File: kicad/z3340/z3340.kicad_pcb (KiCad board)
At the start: 4 copper layers, 80 x 80 mm, 152 parts, among them J1 Conn_01x01, J2 Conn_01x02, J3 Conn_02x20_Odd_Even, Q1 2N7002, Q2 2N7002, Q3 MMBT3904, U1 DG442CY+, U10 AS3364, U11 PCA9555D, U12 AD5328, U13 TL074, U14 DG406, U15 M24C02-WMN, U2 AS3340, U3 LM79L05, U4 LM311, U5 TL074, U6 LM4040AIM3-2.5, U7 LM4040B-5, U8 DG442CY+, U9 TL072

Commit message: continue file renaming
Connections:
- net /cem3340/COMP_OUT renamed /vco3340/COMP_OUT
- net /cem3340/HARD_SYNC renamed /vco3340/HARD_SYNC
- net /cem3340/HIGH_FREQ_TRACK renamed /vco3340/HIGH_FREQ_TRACK
- net /cem3340/LINEAR_FM renamed /vco3340/LINEAR_FM
- net /cem3340/PWM renamed /vco3340/PWM
- net /cem3340/SOFT_SYNC renamed /vco3340/SOFT_SYNC
- net /cem3340/SUMMING_INPUT renamed /vco3340/SUMMING_INPUT
- net /cem3340/VREF_5 renamed /vco3340/VREF_5

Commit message: z3340 v0.8 RTM
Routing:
- net GND: track 206.2 -> 203.9 mm, vias 79 -> 81
- net /VCO_PULSE: track 79.0 -> 77.7 mm
- net -12V: track 55.8 -> 55.0 mm
- net /VCO_SAW: track 74.2 -> 74.8 mm
- net +12V: track 44.4 -> 43.8 mm
- net /DAC/PWM_FROM_DAC: track 30.4 -> 30.9 mm

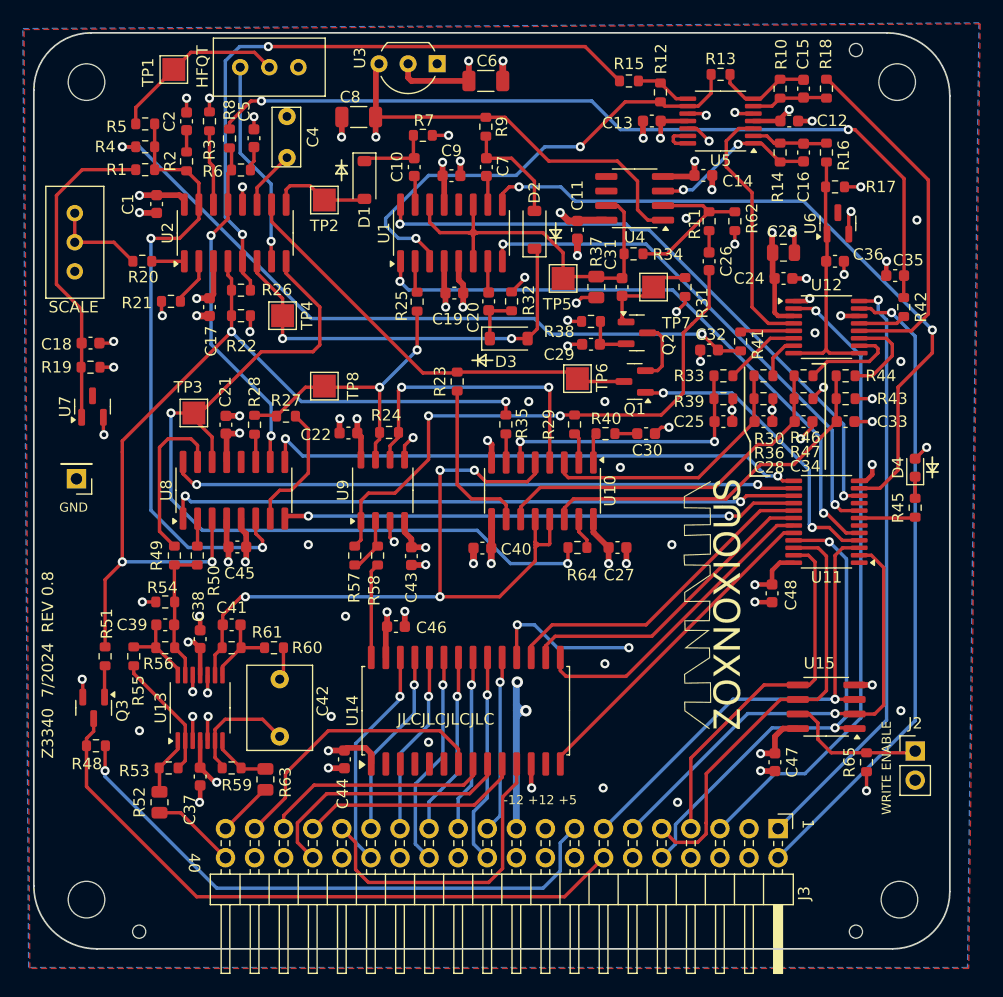
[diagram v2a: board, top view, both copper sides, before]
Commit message: checkpoint for z3340 v0.9.  Fixed lm4040 resistor, exp modulation level; removed polygons from routing
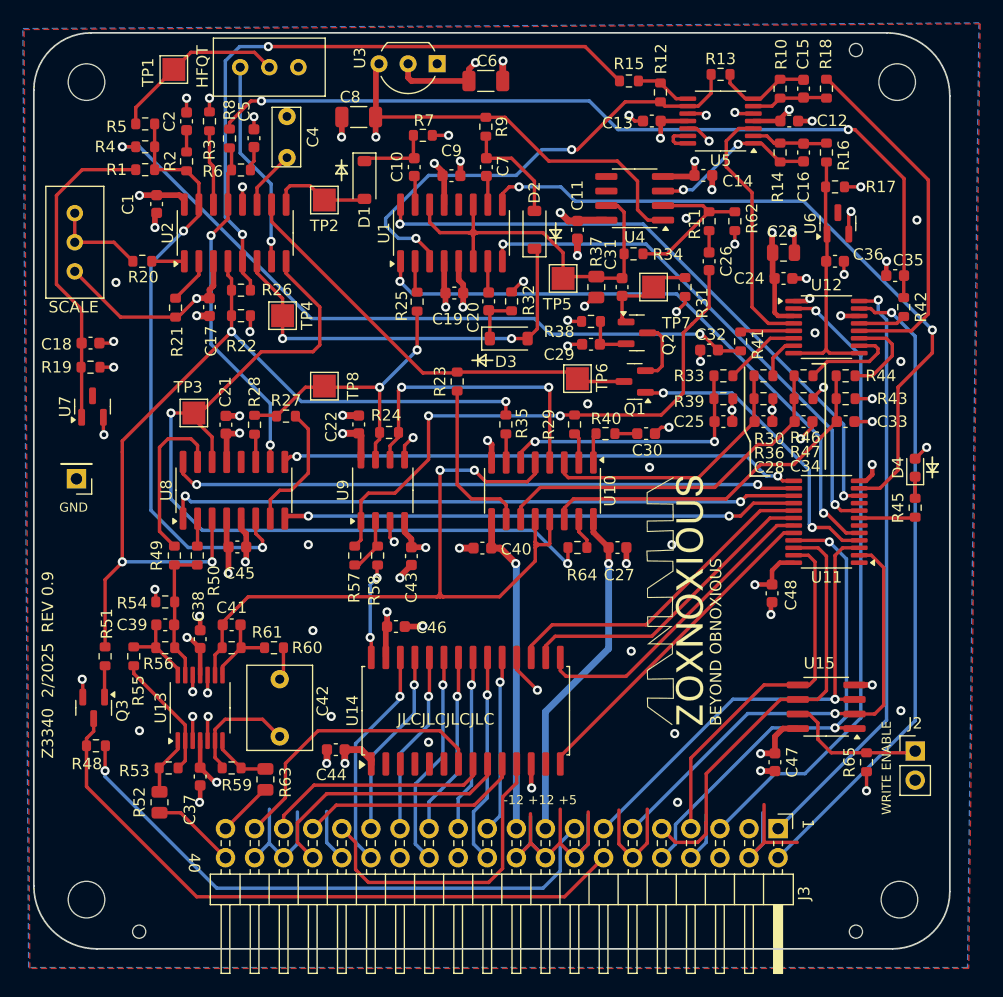
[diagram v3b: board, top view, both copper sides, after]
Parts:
- R17: value 12k -> 10k
- R27: value 200k -> 47k
- R28: value 300k -> 100k
- moved G*** 3.27 mm to (154.6, 120.0)
- moved C22 1.17 mm to (127.0, 104.6), turned to 90 degrees
- moved C44 1.13 mm to (125.0, 133.0), turned to 180 degrees
- moved R21 0.68 mm to (111.0, 94.4), turned to -90 degrees
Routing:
- net +12V: track 43.8 -> 266.8 mm
- net -12V: track 55.0 -> 171.1 mm, vias 11 -> 9
- net GND: track 203.9 -> 314.3 mm, vias 81 -> 80
- net +5V: track 88.1 -> 192.0 mm, vias 9 -> 8
- net -5V: track 42.6 -> 76.5 mm, vias 3 -> 2
- net /LINEAR_FM_EXT_CTRL: track 48.0 -> 45.6 mm
- net /vco3340/SUMMING_INPUT: track 54.0 -> 52.5 mm
- net /PULSE_VCA_AMOUNT_DAC: track 24.6 -> 24.0 mm
- net /CARD7_OUT1: track 25.1 -> 25.7 mm
- net Net-(U10C-Iout): track 63.6 -> 64.0 mm, vias 4 -> 2
- net Net-(U14-D): track 8.30 -> 8.38 mm, vias 0 -> 2
- removed copper zone on In2.Cu, net +12V
- removed copper zone on In2.Cu, net +5V
- removed copper zone on In2.Cu, net -12V
- removed copper zone on In2.Cu, net -5V
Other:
- board text added: "BEYOND OBNOXIOUS"
- board text added: "Z3340 2/2025 REV 0.9"
- board text removed: "Z3340 7/2024 REV 0.8"

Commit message: updates for v0.9: polygons, LED resistor, mod amount
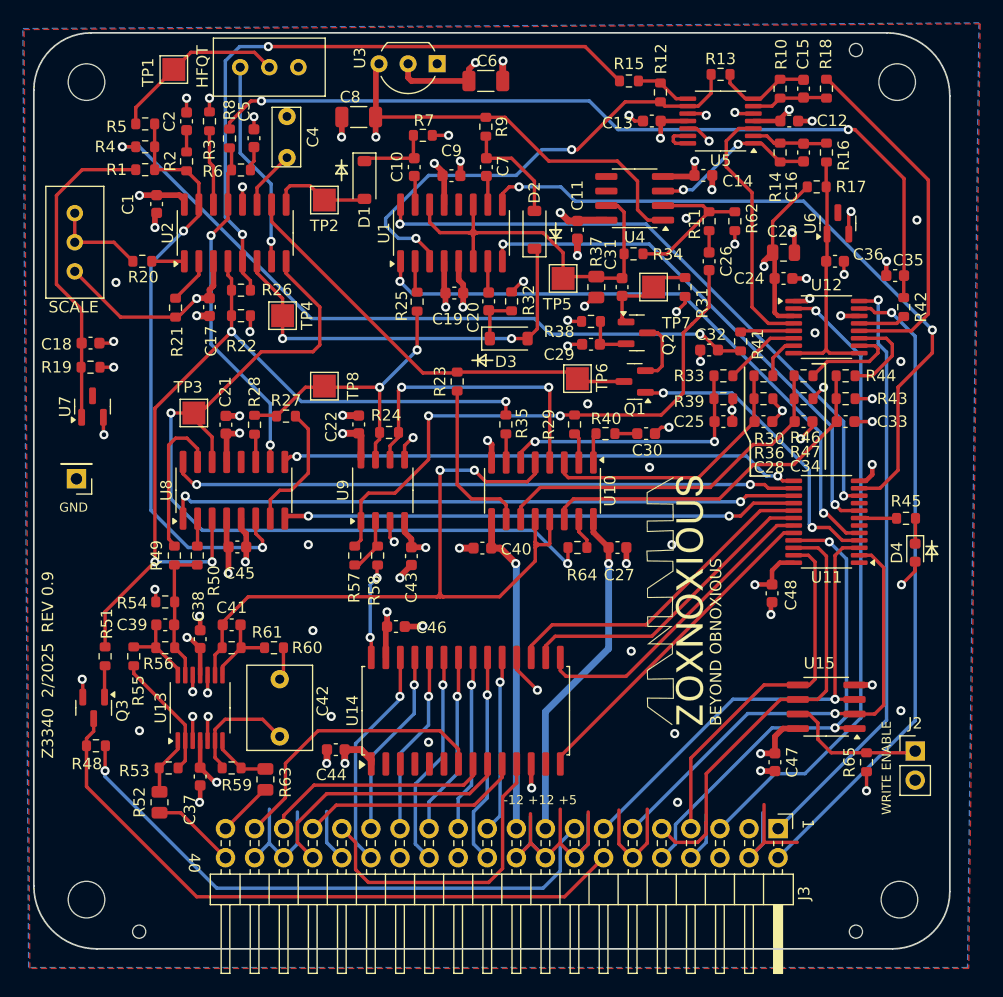
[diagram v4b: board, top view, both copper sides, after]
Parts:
- moved D4 7.42 mm to (175.6, 115.8), turned to -90 degrees
- moved R17 1.60 mm to (167.0, 83.8), turned to 0 degrees
- moved R45 1.22 mm to (174.8, 112.8), turned to 180 degrees
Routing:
- net +5V: track 192.0 -> 183.5 mm, vias 8 -> 7
- net /VCO_PULSE: track 77.7 -> 74.8 mm
- net /LED_CTRL: track 4.92 -> 3.27 mm
- net Net-(R49-Pad1): track 14.5 -> 13.3 mm
- net GND: track 314.3 -> 315.0 mm
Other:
- board text removed: "JLCJLCJLCJLC"

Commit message: routing update on z3340
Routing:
- net -12V: track 171.1 -> 167.9 mm
